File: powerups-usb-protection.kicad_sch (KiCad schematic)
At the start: 2 parts, among them P1 USB_C_Plug_USB2.0, P2 USB_C_Plug_USB2.0

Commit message: First schematic and layout
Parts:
- added Q1: DMN3016LFDE, PowerFeather_KiCAD_Lib:DMN3016LFDE, symbol Device:Q_NMOS_GDS
- added U1: NCV68261, PowerFeather_KiCAD_Lib:DFN-6_2x2mm_P0.65mm_EP1x1.6mm, symbol PowerFeather_KiCAD_Lib:NCV68261
- P1, P2: footprint (none) -> Connector_USB:USB_C_Receptacle_HRO_TYPE-C-31-M-12
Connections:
- net GND: now reaches P2.A1 (GND), P2.A12 (GND), P2.B1 (GND), P2.B12 (GND)
- net GND: now also P1.A1 (GND), P1.A12 (GND), P1.B1 (GND), P1.B12 (GND), U1.5 (GND)
- net at P2.A4 (VBUS), P2.A9 (VBUS), P2.B4 (VBUS)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: now also Q1.3 (S), U1.1 (S), U1.4 (EN), U1.6 (IN)
- net at P2.A5 (CC): now also P1.A5 (CC)
- net at P2.A6 (D+): now also P1.A6 (D+)
- net at P2.A7 (D-): now also P1.A7 (D-)
- net at P2.B5 (VCONN): now also P1.B5 (VCONN)
- net at P2.S1 (SHIELD): now also P1.S1 (SHIELD)
- net at P1.A4 (VBUS), P1.A9 (VBUS), P1.B4 (VBUS)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: now also Q1.2 (D), U1.3 (D)
- new net: Q1.1 (G), U1.2 (G)
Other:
- moved on the sheet: P1, P2

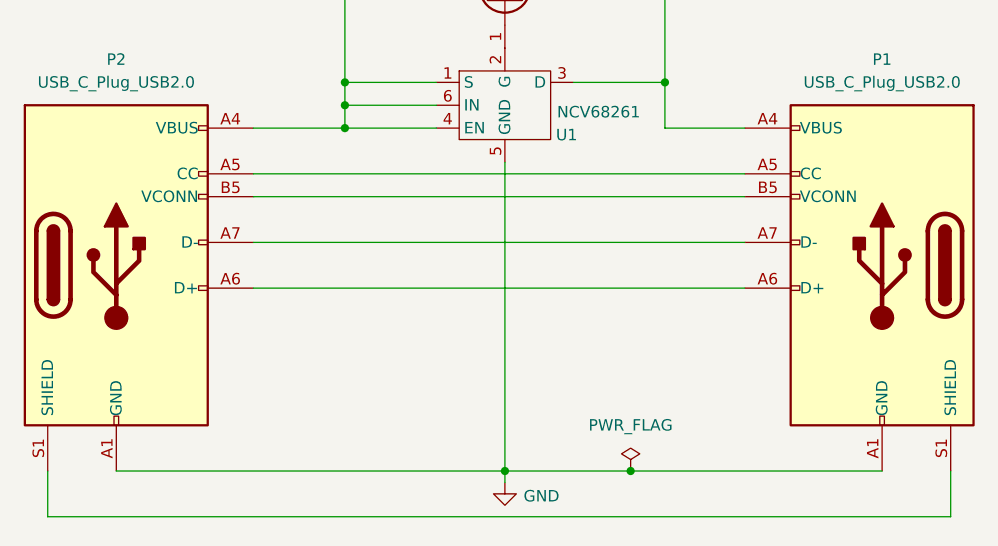
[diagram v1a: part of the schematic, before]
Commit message: Use full receptacle symbol
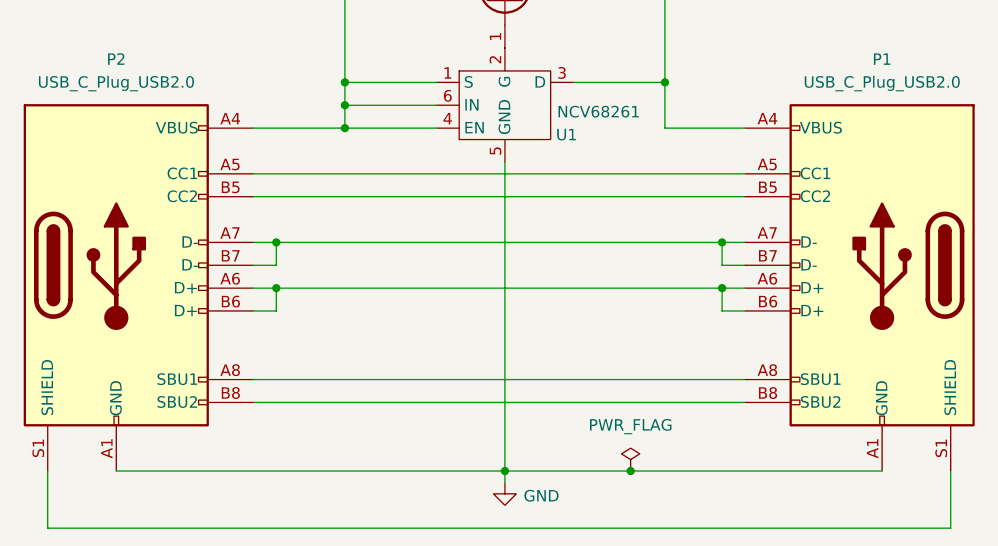
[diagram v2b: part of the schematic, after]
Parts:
- P1, P2: symbol Connector:USB_C_Plug_USB2.0 -> Connector:USB_C_Receptacle_USB2.0_16P
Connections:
- net at P1.A6 (D+), P2.A6 (D+): now also P1.B6 (D+), P2.B6 (D+)
- net at P1.A7 (D-), P2.A7 (D-): now also P1.B7 (D-), P2.B7 (D-)
- new net: P1.A8 (SBU1), P2.A8 (SBU1)
- new net: P1.B8 (SBU2), P2.B8 (SBU2)
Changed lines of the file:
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@@
+	)
+	(junction
+		(at 72.39 58.42)
+		(diameter 0)
+		(color 0 0 0 0)
 	)
 	(junction
@@
 	)
 	(junction
+		(at 72.39 63.5)
+		(diameter 0)
+		(color 0 0 0 0)
+	)
+	(junction
+		(at 121.92 58.42)
+		(diameter 0)
+		(color 0 0 0 0)
+	)
+	(junction
 		(at 97.79 83.82)
 		(diameter 0)
@@
 	)
 	(junction
+		(at 121.92 63.5)
+		(diameter 0)
+		(color 0 0 0 0)
+	)
+	(junction
 		(at 115.57 40.64)
 		(diameter 0)
@@
 	(wire
 		(pts
+			(xy 124.46 60.96) (xy 121.92 60.96)
+		)
+		(stroke
+			(width 0)
+			(type default)
+		)
+	)
+	(wire
+		(pts
+			(xy 121.92 58.42) (xy 124.46 58.42)
+		)
+		(stroke
+			(width 0)
+			(type default)
+		)
+	)
+	(wire
+		(pts
 			(xy 97.79 83.82) (xy 111.76 83.82)
 		)
@@
 	(wire
 		(pts
-			(xy 46.99 83.82) (xy 46.99 88.9)
+			(xy 69.85 60.96) (xy 72.39 60.96)
+		)
+		(stroke
+			(width 0)
+			(type default)
+		)
+	)
+	(wire
+		(pts
+			(xy 46.99 90.17) (xy 46.99 83.82)
 		)
 		(stroke
@@
 	(wire
 		(pts
-			(xy 46.99 88.9) (xy 147.32 88.9)
-		)
-		(stroke
-			(width 0)
-			(type default)
-		)
-	)
-	(wire
-		(pts
 			(xy 97.79 83.82) (xy 97.79 85.09)
 		)
@@
 	(wire
 		(pts
-			(xy 147.32 88.9) (xy 147.32 83.82)
-		)
-		(stroke
-			(width 0)
-			(type default)
-		)
-	)
-	(wire
-		(pts
 			(xy 115.57 45.72) (xy 124.46 45.72)
 		)
@@
 	(wire
 		(pts
+			(xy 72.39 63.5) (xy 121.92 63.5)
+		)
+		(stroke
+			(width 0)
+			(type default)
+		)
+	)
+	(wire
+		(pts
 			(xy 80.01 43.18) (xy 80.01 45.72)
 		)
@@
 	(wire
 		(pts
-			(xy 69.85 58.42) (xy 124.46 58.42)
+			(xy 147.32 83.82) (xy 147.32 90.17)
+		)
+		(stroke
+			(width 0)
+			(type default)
+		)
+	)
+	(wire
+		(pts
+			(xy 72.39 60.96) (xy 72.39 58.42)
+		)
+		(stroke
+			(width 0)
+			(type default)
+		)
+	)
+	(wire
+		(pts
+			(xy 69.85 58.42) (xy 72.39 58.42)
+		)
+		(stroke
+			(width 0)
+			(type default)
+		)
+	)
+	(wire
+		(pts
+			(xy 72.39 66.04) (xy 72.39 63.5)
+		)
+		(stroke
+			(width 0)
+			(type default)
+		)
+	)
+	(wire
+		(pts
+			(xy 69.85 73.66) (xy 124.46 73.66)
 		)
 		(stroke
@@
 	(wire
 		(pts
+			(xy 147.32 90.17) (xy 46.99 90.17)
+		)
+		(stroke
+			(width 0)
+			(type default)
+		)
+	)
+	(wire
+		(pts
 			(xy 115.57 29.21) (xy 115.57 40.64)
 		)
@@
 	(wire
 		(pts
+			(xy 121.92 66.04) (xy 121.92 63.5)
+		)
+		(stroke
+			(width 0)
+			(type default)
+		)
+	)
+	(wire
+		(pts
 			(xy 115.57 40.64) (xy 115.57 45.72)
 		)
@@
 	(wire
 		(pts
+			(xy 124.46 66.04) (xy 121.92 66.04)
+		)
+		(stroke
+			(width 0)
+			(type default)
+		)
+	)
+	(wire
+		(pts
+			(xy 121.92 63.5) (xy 124.46 63.5)
+		)
+		(stroke
+			(width 0)
+			(type default)
+		)
+	)
+	(wire
+		(pts
+			(xy 121.92 60.96) (xy 121.92 58.42)
+		)
+		(stroke
+			(width 0)
+			(type default)
+		)
+	)
+	(wire
+		(pts
+			(xy 72.39 58.42) (xy 121.92 58.42)
+		)
+		(stroke
+			(width 0)
+			(type default)
+		)
+	)
+	(wire
+		(pts
+			(xy 69.85 66.04) (xy 72.39 66.04)
+		)
+		(stroke
+			(width 0)
+			(type default)
+		)
+	)
+	(wire
+		(pts
 			(xy 80.01 43.18) (xy 90.17 43.18)
 		)
@@
 	(wire
 		(pts
+			(xy 69.85 76.2) (xy 124.46 76.2)
+		)
+		(stroke
+			(width 0)
+			(type default)
+		)
+	)
+	(wire
+		(pts
 			(xy 111.76 83.82) (xy 139.7 83.82)
 		)
@@
 	(wire
 		(pts
-			(xy 69.85 63.5) (xy 124.46 63.5)
+			(xy 69.85 63.5) (xy 72.39 63.5)
 		)
 		(stroke
@@
 	)
 	(symbol
-		(lib_id "Connector:USB_C_Plug_USB2.0")
+		(lib_id "Connector:USB_C_Receptacle_USB2.0_16P")
 		(at 54.61 60.96 0)
 		(unit 1)
@@
 			)
 		)
-		(property "Description" "USB 2.0-only Type-C Plug connector"
+		(property "Description" "USB 2.0-only 16P Type-C Receptacle connector"
 			(at 54.61 60.96 0)
 			(effects
@@
 		)
 		(pin "A1"
+		)
+		(pin "B7"
+		)
+		(pin "A8"
+		)
+		(pin "B8"
+		)
+		(pin "B6"
 		)
 		(instances
@@
 	)
 	(symbol
-		(lib_id "Connector:USB_C_Plug_USB2.0")
+		(lib_id "Connector:USB_C_Receptacle_USB2.0_16P")
 		(at 139.7 60.96 0)
 		(mirror y)
@@
 			)
 		)
-		(property "Description" "USB 2.0-only Type-C Plug connector"
+		(property "Description" "USB 2.0-only 16P Type-C Receptacle connector"
 			(at 139.7 60.96 0)
 			(effects
@@
 		(pin "A1"
 		)
+		(pin "B7"
+		)
+		(pin "B6"
+		)
+		(pin "B8"
+		)
+		(pin "A8"
+		)
 		(instances

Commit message: Set part numbers
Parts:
- P1, P2: MPN (none) -> 640-USB4105-GF-A-060
- U1: MPN (none) -> 863-NCV68261MTWAITBG
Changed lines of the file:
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@@
+			)
+		)
+		(property "MPN" "863-NCV68261MTWAITBG "
+			(at 97.79 44.45 0)
+			(effects
+				(font
+					(size 1.27 1.27)
+				)
+				(hide yes)
 			)
 		)
@@
 		)
 		(property "Description" "USB 2.0-only 16P Type-C Receptacle connector"
+			(at 54.61 60.96 0)
+			(effects
+				(font
+					(size 1.27 1.27)
+				)
+				(hide yes)
+			)
+		)
+		(property "MPN" "640-USB4105-GF-A-060 "
 			(at 54.61 60.96 0)
 			(effects
@@
 			(at 139.7 60.96 0)
 			(effects
+				(font
+					(size 1.27 1.27)
+				)
+				(hide yes)
+			)
+		)
+		(property "MPN" "640-USB4105-GF-A-060 "
+			(at 139.7 60.96 0)
+			(effects

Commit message: Prepare for fabrication
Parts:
- P1, P2: MPN 640-USB4105-GF-A-060 -> 640-USB4105-GF-A-060
- U1: MPN 863-NCV68261MTWAITBG -> 863-NCV68261MTWAITBG
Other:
- company: (none) -> PowerFeather
- title: (none) -> PowerUPS USB Supply Protection

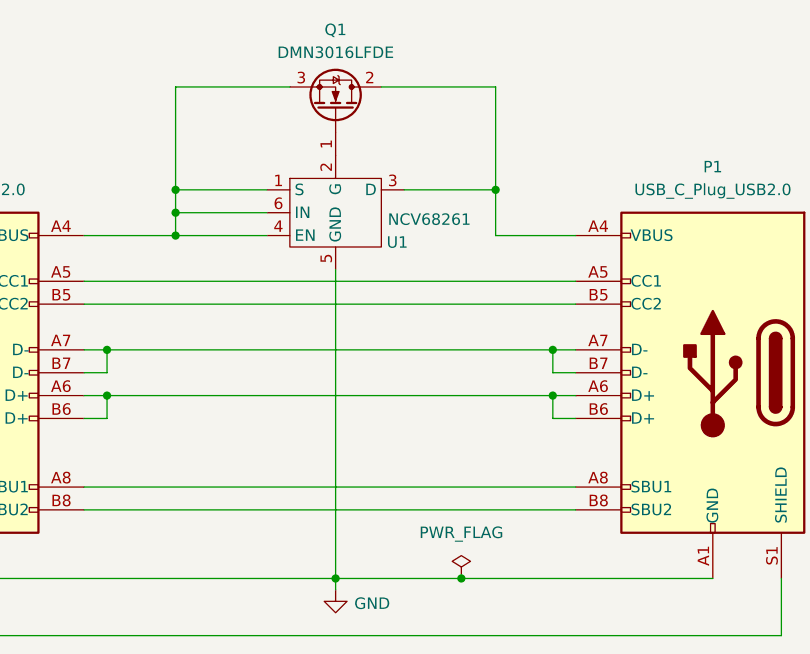
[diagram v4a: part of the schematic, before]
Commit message: Fix ncv68261 footprint and symbol
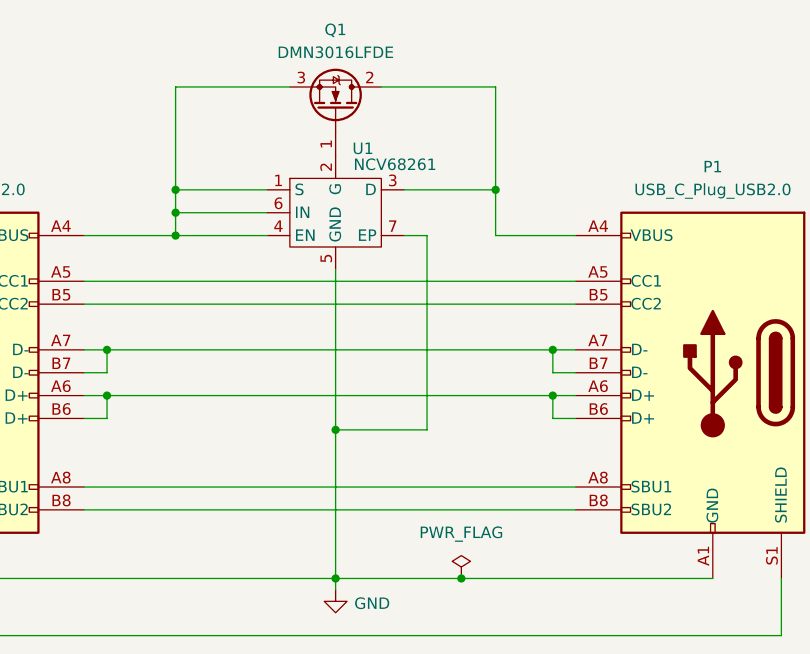
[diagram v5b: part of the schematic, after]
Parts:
- U1: footprint PowerFeather_KiCAD_Lib:DFN-6_2x2mm_P0.65mm_EP1x1.6mm -> Package_DFN_QFN:DFN-6-1EP_2x2mm_P0.65mm_EP1x1.6mm
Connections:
- net GND: now also U1.7 (EP)
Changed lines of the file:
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@@
+	)
+	(junction
+		(at 97.79 67.31)
+		(diameter 0)
+		(color 0 0 0 0)
 	)
 	(junction
@@
 	(wire
 		(pts
+			(xy 105.41 45.72) (xy 107.95 45.72)
+		)
+		(stroke
+			(width 0)
+			(type default)
+		)
+	)
+	(wire
+		(pts
 			(xy 80.01 40.64) (xy 80.01 43.18)
 		)
@@
 	(wire
 		(pts
+			(xy 107.95 67.31) (xy 97.79 67.31)
+		)
+		(stroke
+			(width 0)
+			(type default)
+		)
+	)
+	(wire
+		(pts
 			(xy 80.01 43.18) (xy 80.01 45.72)
 		)
@@
 	(wire
 		(pts
+			(xy 97.79 67.31) (xy 97.79 83.82)
+		)
+		(stroke
+			(width 0)
+			(type default)
+		)
+	)
+	(wire
+		(pts
 			(xy 72.39 60.96) (xy 72.39 58.42)
 		)
@@
 	(wire
 		(pts
+			(xy 107.95 45.72) (xy 107.95 67.31)
+		)
+		(stroke
+			(width 0)
+			(type default)
+		)
+	)
+	(wire
+		(pts
 			(xy 69.85 73.66) (xy 124.46 73.66)
 		)
@@
 	(wire
 		(pts
-			(xy 97.79 49.53) (xy 97.79 83.82)
+			(xy 97.79 49.53) (xy 97.79 67.31)
 		)
 		(stroke
@@
 		(dnp no)
 		(property "Reference" "U1"
-			(at 104.648 46.482 0)
+			(at 100.838 36.068 0)
 			(effects
 				(font
@@
 		)
 		(property "Value" "NCV68261"
-			(at 108.204 43.942 0)
+			(at 104.394 37.846 0)
 			(effects
 				(font
@@
 			)
 		)
-		(property "Footprint" "PowerFeather_KiCAD_Lib:DFN-6_2x2mm_P0.65mm_EP1x1.6mm"
+		(property "Footprint" "Package_DFN_QFN:DFN-6-1EP_2x2mm_P0.65mm_EP1x1.6mm"
 			(at 97.79 55.118 0)
 			(effects
@@
 		(pin "3"
 		)
+		(pin "7"
+		)
 		(instances

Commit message: Update version
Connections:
- net GND: no longer U1.7 (EP)
- no-connect marks 0 -> 1
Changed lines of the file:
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@@
 		(title "PowerUPS USB Supply Protection")
 		(date "2024-10-27")
-		(rev "0.9.0")
+		(rev "0.9.1")
 		(company "PowerFeather")
 	)
@@
 	)
 	(junction
-		(at 97.79 67.31)
-		(diameter 0)
-		(color 0 0 0 0)
-	)
-	(junction
 		(at 121.92 63.5)
 		(diameter 0)
@@
 		(color 0 0 0 0)
 	)
+	(no_connect
+		(at 105.41 45.72)
+	)
 	(wire
 		(pts
@@
 	(wire
 		(pts
-			(xy 105.41 45.72) (xy 107.95 45.72)
-		)
-		(stroke
-			(width 0)
-			(type default)
-		)
-	)
-	(wire
-		(pts
 			(xy 80.01 40.64) (xy 80.01 43.18)
 		)
@@
 	(wire
 		(pts
-			(xy 107.95 67.31) (xy 97.79 67.31)
-		)
-		(stroke
-			(width 0)
-			(type default)
-		)
-	)
-	(wire
-		(pts
 			(xy 80.01 43.18) (xy 80.01 45.72)
 		)
@@
 	(wire
 		(pts
-			(xy 97.79 67.31) (xy 97.79 83.82)
+			(xy 97.79 49.53) (xy 97.79 83.82)
 		)
 		(stroke
@@
 	(wire
 		(pts
-			(xy 107.95 45.72) (xy 107.95 67.31)
-		)
-		(stroke
-			(width 0)
-			(type default)
-		)
-	)
-	(wire
-		(pts
 			(xy 69.85 73.66) (xy 124.46 73.66)
 		)
@@
 		)
 		(stroke
-			(width 0)
-			(type default)
-		)
-	)
-	(wire
-		(pts
-			(xy 97.79 49.53) (xy 97.79 67.31)
-		)
-		(stroke
